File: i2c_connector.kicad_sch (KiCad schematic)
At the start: 10 parts, among them J3 SM04B-SRSS-TB(LF)(SN)

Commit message: Optimise routes, add caps
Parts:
- added C7 (x2): 15uF, Capacitor_SMD:C_1210_3225Metric_Pad1.33x2.70mm_HandSolder, symbol Device:C_Small
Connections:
- net +5V: now also C7.2, C7.2
- net GND: now also C7.1, C7.1
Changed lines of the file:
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@@
     (stroke (width 0) (type solid))
+  )
+  (wire (pts (xy 71.12 81.28) (xy 71.12 86.36))
+    (stroke (width 0) (type default))
   )
   (wire (pts (xy 162.56 95.25) (xy 162.56 97.79))
@@
     (stroke (width 0) (type default))
   )
+  (wire (pts (xy 54.61 72.39) (xy 54.61 77.47))
+    (stroke (width 0) (type default))
+  )
   (wire (pts (xy 85.09 71.12) (xy 85.09 76.2))
     (stroke (width 0) (type default))
@@
     (stroke (width 0) (type solid))
   )
+  (wire (pts (xy 54.61 82.55) (xy 54.61 87.63))
+    (stroke (width 0) (type default))
+  )
   (wire (pts (xy 172.72 153.67) (xy 157.48 153.67))
     (stroke (width 0) (type default))
   )
   (wire (pts (xy 154.94 125.73) (xy 154.94 130.81))
+    (stroke (width 0) (type default))
+  )
+  (wire (pts (xy 71.12 71.12) (xy 71.12 76.2))
     (stroke (width 0) (type default))
   )
@@
         (path "/eed35b77-cbf9-4596-9b17-2558f81058ba/eeffdcd2-f49f-4c6e-9443-50950813e7b1"
           (reference "C6") (unit 1)
+        )
+      )
+    )
+  )
+  (symbol (lib_id "Device:C_Small") (at 71.12 78.74 180) (unit 1)
+    (in_bom yes) (on_board yes) (dnp no)
+    (property "Reference" "C7" (at 76.2 77.47 0)
+      (effects (font (size 1.27 1.27)))
+    )
+    (property "Value" "15uF" (at 76.2 80.01 0)
+      (effects (font (size 1.27 1.27)))
+    )
+    (property "Footprint" "Capacitor_SMD:C_1210_3225Metric_Pad1.33x2.70mm_HandSolder" (at 71.12 78.74 0)
+      (effects (font (size 1.27 1.27)) hide)
+    )
+    (property "Datasheet" "~" (at 71.12 78.74 0)
+      (effects (font (size 1.27 1.27)) hide)
+    )
+    (pin "1")
+    (pin "2")
+    (instances
+      (project "LTP305_ESP32_CLOCK"
+        (path "/c007e288-8439-49d9-bbdf-49724c34958c"
+          (reference "C7") (unit 1)
+        )
+      )
+      (project "ltp_kikad"
+        (path "/eed35b77-cbf9-4596-9b17-2558f81058ba"
+          (reference "C6") (unit 1)
+        )
+        (path "/eed35b77-cbf9-4596-9b17-2558f81058ba/eeffdcd2-f49f-4c6e-9443-50950813e7b1"
+          (reference "C10") (unit 1)
         )
       )
@@
     )
   )
+  (symbol (lib_id "power:+5V") (at 71.12 71.12 0) (unit 1)
+    (in_bom yes) (on_board yes) (dnp no)
+    (property "Reference" "#PWR08" (at 71.12 74.93 0)
+      (effects (font (size 1.27 1.27)) hide)
+    )
+    (property "Value" "+5V" (at 71.501 66.7258 0)
+      (effects (font (size 1.27 1.27)))
+    )
+    (property "Footprint" "" (at 71.12 71.12 0)
+      (effects (font (size 1.27 1.27)) hide)
+    )
+    (property "Datasheet" "" (at 71.12 71.12 0)
+      (effects (font (size 1.27 1.27)) hide)
+    )
+    (pin "1")
+    (instances
+      (project "LTP305_ESP32_CLOCK"
+        (path "/c007e288-8439-49d9-bbdf-49724c34958c"
+          (reference "#PWR08") (unit 1)
+        )
+      )
+      (project "ltp_kikad"
+        (path "/eed35b77-cbf9-4596-9b17-2558f81058ba"
+          (reference "#PWR08") (unit 1)
+        )
+        (path "/eed35b77-cbf9-4596-9b17-2558f81058ba/eeffdcd2-f49f-4c6e-9443-50950813e7b1"
+          (reference "#PWR034") (unit 1)
+        )
+      )
+    )
+  )
+  (symbol (lib_id "power:GND") (at 71.12 86.36 0) (unit 1)
+    (in_bom yes) (on_board yes) (dnp no)
+    (property "Reference" "#PWR033" (at 71.12 92.71 0)
+      (effects (font (size 1.27 1.27)) hide)
+    )
+    (property "Value" "GND" (at 71.247 90.7542 0)
+      (effects (font (size 1.27 1.27)))
+    )
+    (property "Footprint" "" (at 71.12 86.36 0)
+      (effects (font (size 1.27 1.27)) hide)
+    )
+    (property "Datasheet" "" (at 71.12 86.36 0)
+      (effects (font (size 1.27 1.27)) hide)
+    )
+    (pin "1")
+    (instances
+      (project "LTP305_ESP32_CLOCK"
+        (path "/c007e288-8439-49d9-bbdf-49724c34958c"
+          (reference "#PWR033") (unit 1)
+        )
+      )
+      (project "ltp_kikad"
+        (path "/eed35b77-cbf9-4596-9b17-2558f81058ba"
+          (reference "#PWR09") (unit 1)
+        )
+        (path "/eed35b77-cbf9-4596-9b17-2558f81058ba/eeffdcd2-f49f-4c6e-9443-50950813e7b1"
+          (reference "#PWR035") (unit 1)
+        )
+      )
+    )
+  )
+  (symbol (lib_id "Device:C_Small") (at 54.61 80.01 180) (unit 1)
+    (in_bom yes) (on_board yes) (dnp no)
+    (property "Reference" "C7" (at 59.69 78.74 0)
+      (effects (font (size 1.27 1.27)))
+    )
+    (property "Value" "15uF" (at 59.69 81.28 0)
+      (effects (font (size 1.27 1.27)))
+    )
+    (property "Footprint" "Capacitor_SMD:C_1210_3225Metric_Pad1.33x2.70mm_HandSolder" (at 54.61 80.01 0)
+      (effects (font (size 1.27 1.27)) hide)
+    )
+    (property "Datasheet" "~" (at 54.61 80.01 0)
+      (effects (font (size 1.27 1.27)) hide)
+    )
+    (pin "1")
+    (pin "2")
+    (instances
+      (project "LTP305_ESP32_CLOCK"
+        (path "/c007e288-8439-49d9-bbdf-49724c34958c"
+          (reference "C7") (unit 1)
+        )
+      )
+      (project "ltp_kikad"
+        (path "/eed35b77-cbf9-4596-9b17-2558f81058ba"
+          (reference "C6") (unit 1)
+        )
+        (path "/eed35b77-cbf9-4596-9b17-2558f81058ba/eeffdcd2-f49f-4c6e-9443-50950813e7b1"
+          (reference "C11") (unit 1)
+        )
+      )
+    )
+  )
   (symbol (lib_id "power:GND") (at 85.09 86.36 0) (unit 1)
     (in_bom yes) (on_board yes) (dnp no)
@@
         (path "/eed35b77-cbf9-4596-9b17-2558f81058ba/eeffdcd2-f49f-4c6e-9443-50950813e7b1"
           (reference "#PWR032") (unit 1)
+        )
+      )
+    )
+  )
+  (symbol (lib_id "power:+5V") (at 54.61 72.39 0) (unit 1)
+    (in_bom yes) (on_board yes) (dnp no)
+    (property "Reference" "#PWR08" (at 54.61 76.2 0)
+      (effects (font (size 1.27 1.27)) hide)
+    )
+    (property "Value" "+5V" (at 54.991 67.9958 0)
+      (effects (font (size 1.27 1.27)))
+    )
+    (property "Footprint" "" (at 54.61 72.39 0)
+      (effects (font (size 1.27 1.27)) hide)
+    )
+    (property "Datasheet" "" (at 54.61 72.39 0)
+      (effects (font (size 1.27 1.27)) hide)
+    )
+    (pin "1")
+    (instances
+      (project "LTP305_ESP32_CLOCK"
+        (path "/c007e288-8439-49d9-bbdf-49724c34958c"
+          (reference "#PWR08") (unit 1)
+        )
+      )
+      (project "ltp_kikad"
+        (path "/eed35b77-cbf9-4596-9b17-2558f81058ba"
+          (reference "#PWR08") (unit 1)
+        )
+        (path "/eed35b77-cbf9-4596-9b17-2558f81058ba/eeffdcd2-f49f-4c6e-9443-50950813e7b1"
+          (reference "#PWR036") (unit 1)
         )
       )
@@
         )
       )
+    )
+  )
+  (symbol (lib_id "power:GND") (at 54.61 87.63 0) (unit 1)
+    (in_bom yes) (on_board yes) (dnp no)
+    (property "Reference" "#PWR033" (at 54.61 93.98 0)
+      (effects (font (size 1.27 1.27)) hide)
+    )
+    (property "Value" "GND" (at 54.737 92.0242 0)
+      (effects (font (size 1.27 1.27)))
+    )
+    (property "Footprint" "" (at 54.61 87.63 0)
+      (effects (font (size 1.27 1.27)) hide)
+    )
+    (property "Datasheet" "" (at 54.61 87.63 0)
+      (effects (font (size 1.27 1.27)) hide)
+    )
+    (pin "1")
+    (instances
+      (project "LTP305_ESP32_CLOCK"
+        (path "/c007e288-8439-49d9-bbdf-49724c34958c"
+          (reference "#PWR033") (unit 1)
+        )
+      )
+      (project "ltp_kikad"
+        (path "/eed35b77-cbf9-4596-9b17-2558f81058ba"
+          (reference "#PWR09") (unit 1)
+        )
+        (path "/eed35b77-cbf9-4596-9b17-2558f81058ba/eeffdcd2-f49f-4c6e-9443-50950813e7b1"
+          (reference "#PWR037") (unit 1)
+        )
+      )

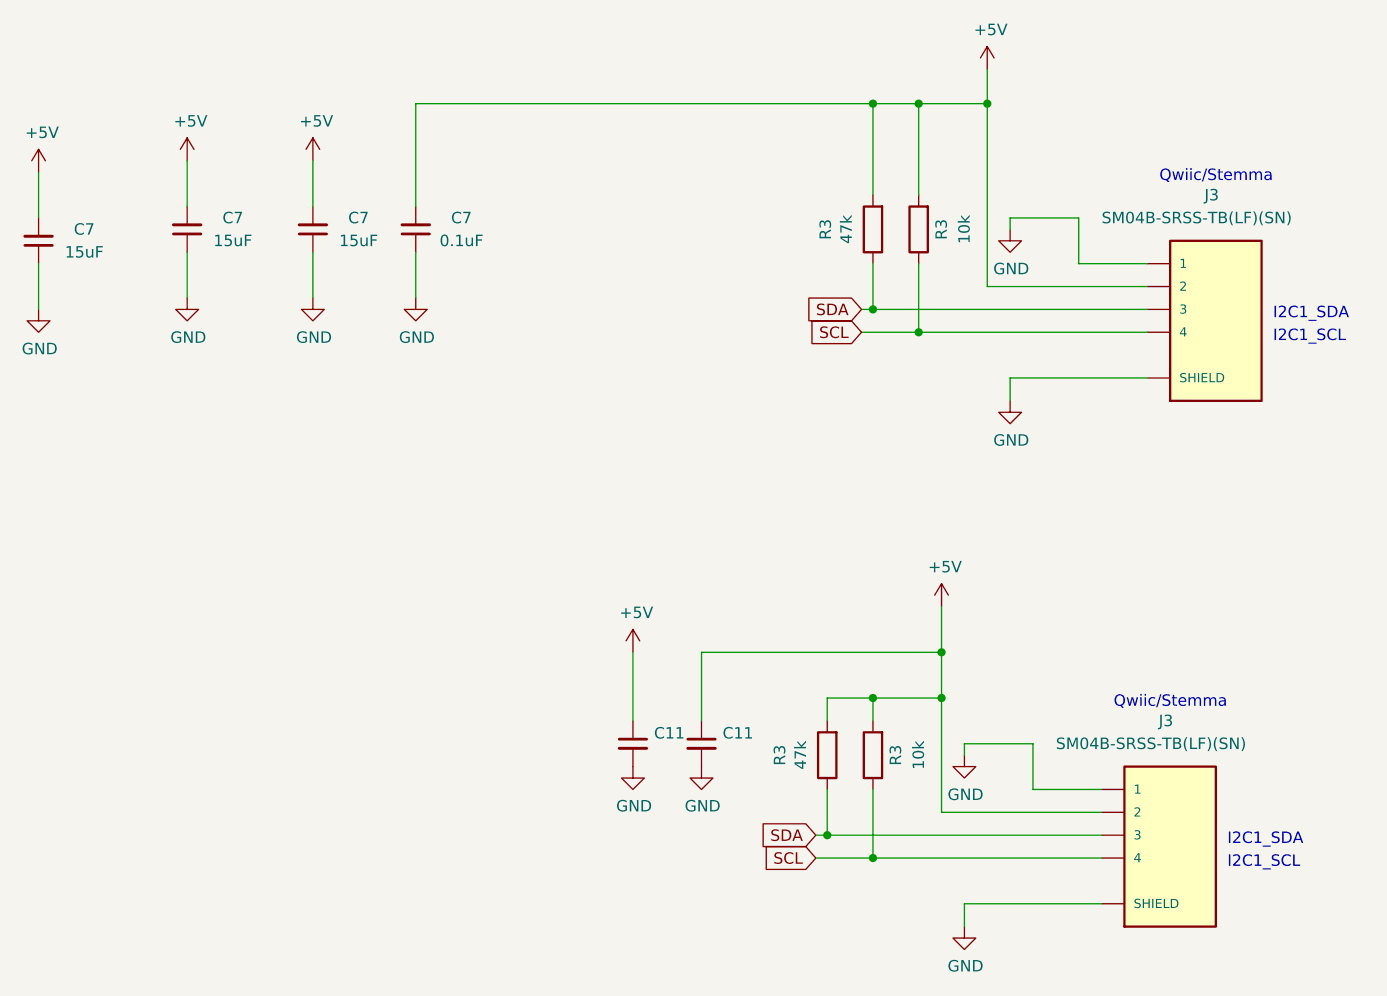
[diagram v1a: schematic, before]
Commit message: Add inductor
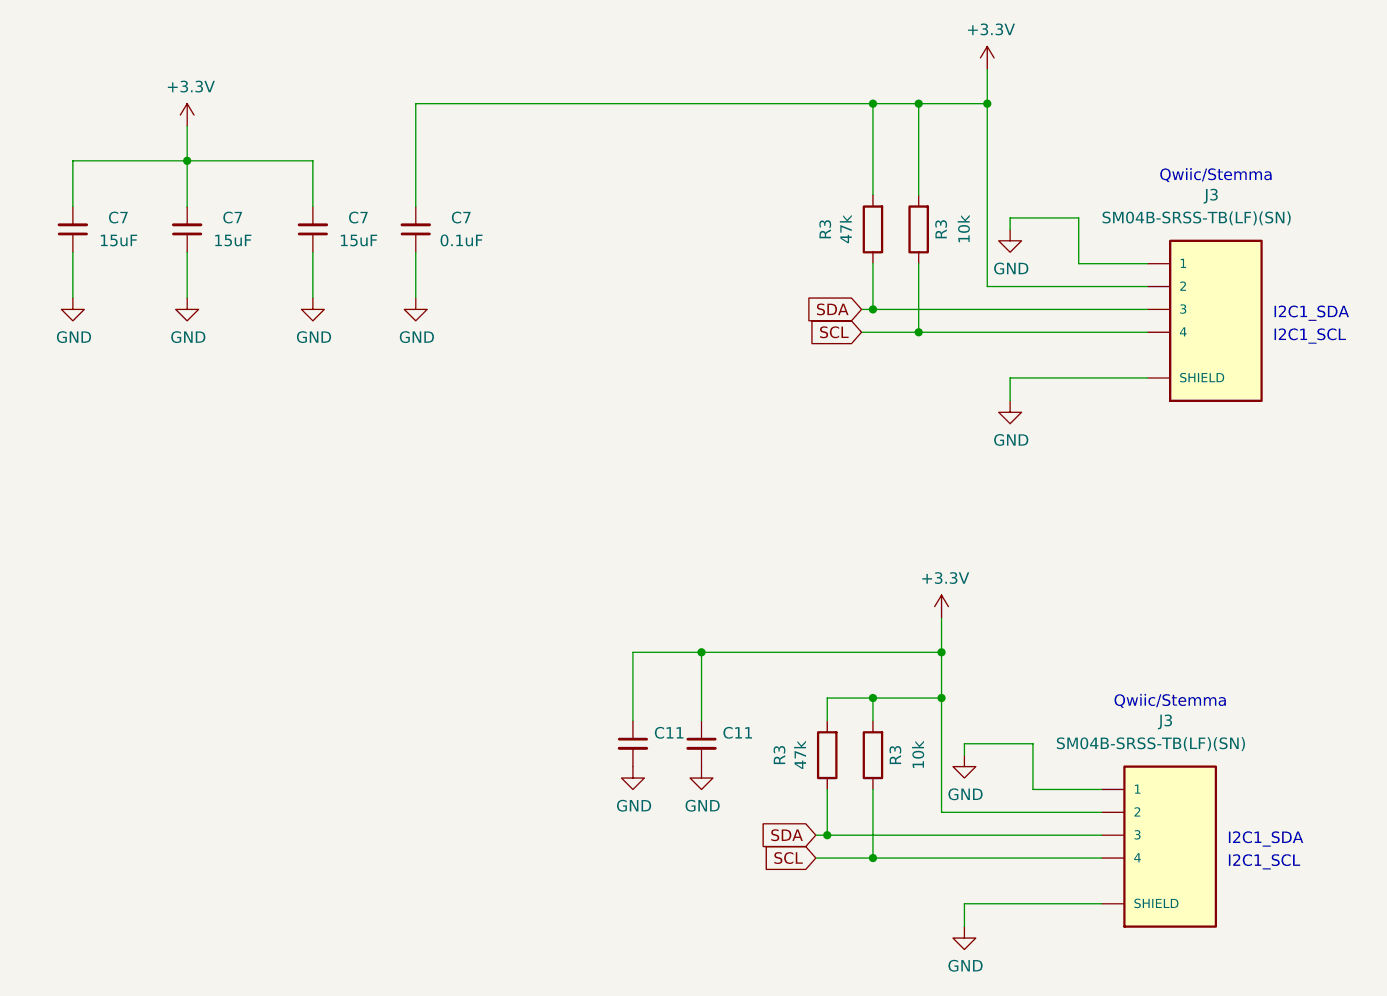
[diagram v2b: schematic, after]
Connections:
- net +5V renamed +3V3
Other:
- moved on the sheet: C7

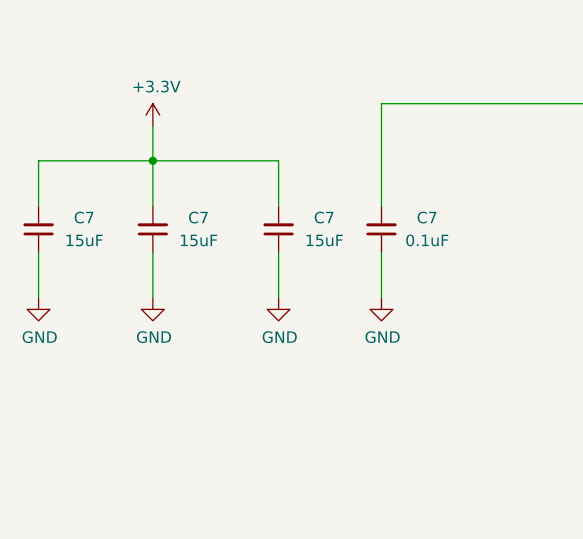
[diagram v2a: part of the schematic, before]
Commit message: Add dc-dc 3.3v to 5v
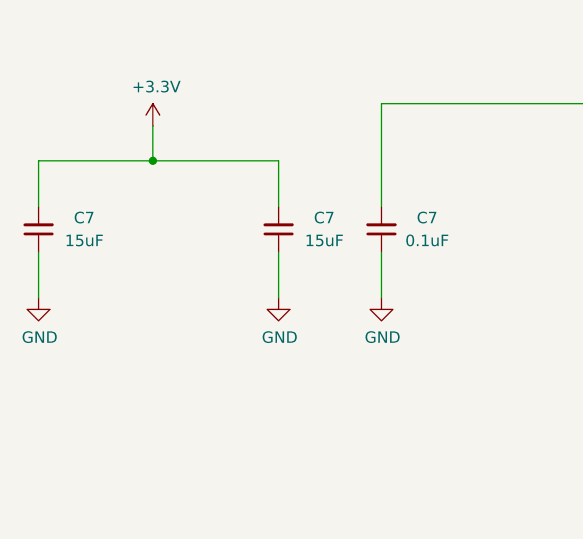
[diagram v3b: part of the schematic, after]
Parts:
- removed C7: 15uF, Capacitor_SMD:C_1210_3225Metric_Pad1.33x2.70mm_HandSolder, symbol Device:C_Small
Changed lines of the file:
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@@
-    (stroke (width 0) (type default))
-  )
-  (wire (pts (xy 71.12 81.28) (xy 71.12 86.36))
     (stroke (width 0) (type default))
   )
@@
   )
   (wire (pts (xy 154.94 125.73) (xy 154.94 130.81))
-    (stroke (width 0) (type default))
-  )
-  (wire (pts (xy 71.12 71.12) (xy 71.12 76.2))
     (stroke (width 0) (type default))
   )
@@
         (path "/eed35b77-cbf9-4596-9b17-2558f81058ba/eeffdcd2-f49f-4c6e-9443-50950813e7b1"
           (reference "C6") (unit 1)
-        )
-      )
-    )
-  )
-  (symbol (lib_id "Device:C_Small") (at 71.12 78.74 180) (unit 1)
-    (in_bom yes) (on_board yes) (dnp no)
-    (property "Reference" "C7" (at 76.2 77.47 0)
-      (effects (font (size 1.27 1.27)))
-    )
-    (property "Value" "15uF" (at 76.2 80.01 0)
-      (effects (font (size 1.27 1.27)))
-    )
-    (property "Footprint" "Capacitor_SMD:C_1210_3225Metric_Pad1.33x2.70mm_HandSolder" (at 71.12 78.74 0)
-      (effects (font (size 1.27 1.27)) hide)
-    )
-    (property "Datasheet" "~" (at 71.12 78.74 0)
-      (effects (font (size 1.27 1.27)) hide)
-    )
-    (pin "1")
-    (pin "2")
-    (instances
-      (project "LTP305_ESP32_CLOCK"
-        (path "/c007e288-8439-49d9-bbdf-49724c34958c"
-          (reference "C7") (unit 1)
-        )
-      )
-      (project "ltp_kikad"
-        (path "/eed35b77-cbf9-4596-9b17-2558f81058ba"
-          (reference "C6") (unit 1)
-        )
-        (path "/eed35b77-cbf9-4596-9b17-2558f81058ba/eeffdcd2-f49f-4c6e-9443-50950813e7b1"
-          (reference "C10") (unit 1)
         )
       )
@@
         )
       )
-    )
-  )
-  (symbol (lib_id "power:GND") (at 71.12 86.36 0) (unit 1)
-    (in_bom yes) (on_board yes) (dnp no)
-    (property "Reference" "#PWR033" (at 71.12 92.71 0)
-      (effects (font (size 1.27 1.27)) hide)
-    )
-    (property "Value" "GND" (at 71.247 90.7542 0)
-      (effects (font (size 1.27 1.27)))
-    )
-    (property "Footprint" "" (at 71.12 86.36 0)
-      (effects (font (size 1.27 1.27)) hide)
-    )
-    (property "Datasheet" "" (at 71.12 86.36 0)
-      (effects (font (size 1.27 1.27)) hide)
-    )
-    (pin "1")
-    (instances
-      (project "LTP305_ESP32_CLOCK"
-        (path "/c007e288-8439-49d9-bbdf-49724c34958c"
-          (reference "#PWR033") (unit 1)
-        )
-      )
-      (project "ltp_kikad"
-        (path "/eed35b77-cbf9-4596-9b17-2558f81058ba"
-          (reference "#PWR09") (unit 1)
-        )
-        (path "/eed35b77-cbf9-4596-9b17-2558f81058ba/eeffdcd2-f49f-4c6e-9443-50950813e7b1"
-          (reference "#PWR035") (unit 1)
-        )
-      )

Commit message: Add title block
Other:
- company: (none) -> Andrew Tudoroi
- title: (none) -> Pitanga HAT
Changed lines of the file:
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@@
 (kicad_sch (version 20230121) (generator eeschema)
   (paper "A4")
+  (title_block
+    (title "Pitanga HAT")
+    (date "2023-10-20")
+    (rev "2.1")
+    (company "Andrew Tudoroi")
+  )
   (junction (at 128.27 125.73) (diameter 0) (color 0 0 0 0)
   )
